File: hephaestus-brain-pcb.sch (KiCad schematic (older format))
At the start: 10 parts, among them J1 Barrel_Jack, J2 ItsyBitsy, J3 ItsyBitsy, J4 Conn_01x03_Male, J5 Conn_01x03_Male, J6 Conn_01x03_Male, J7 Conn_01x03_Male, U1 74126

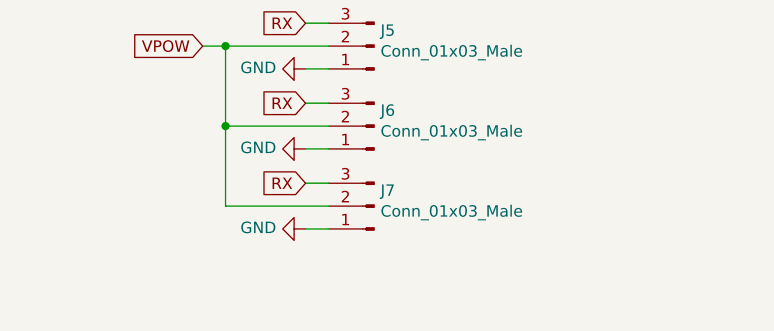
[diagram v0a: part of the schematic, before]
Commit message: Added homing switch connector
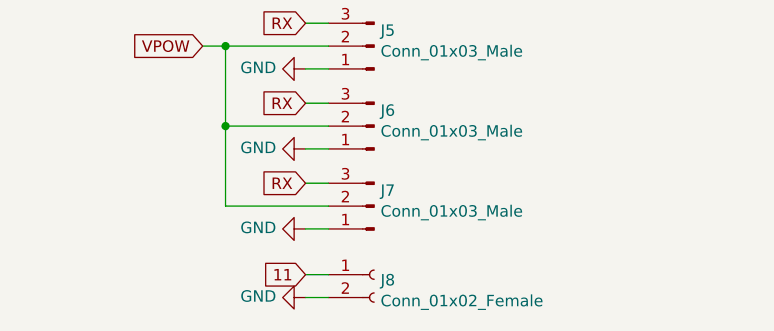
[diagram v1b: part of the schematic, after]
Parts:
- added J8: Conn_01x02_Female, Connector_PinSocket_2.54mm:PinSocket_1x02_P2.54mm_Vertical, symbol Connector:Conn_01x02_Female
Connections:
- net 11: now also J8.1 (Pin_1)
- net GND: now also J8.2 (Pin_2)
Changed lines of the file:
@@
 	4300 4850 4750 4850
 Connection ~ 4300 4500
+$Comp
+L Connector:Conn_01x02_Female J8
+U 1 1 5F188735
+P 4950 5150
+F 0 "J8" H 4978 5126 50  0000 L CNN
+F 1 "Conn_01x02_Female" H 4978 5035 50  0000 L CNN
+F 2 "Connector_PinSocket_2.54mm:PinSocket_1x02_P2.54mm_Vertical" H 4950 5150 50  0001 C CNN
+F 3 "~" H 4950 5150 50  0001 C CNN
+	1    4950 5150
+	1    0    0    -1
+$EndComp
+$Comp
+L power:GND #PWR0104
+U 1 1 5F18915B
+P 4650 5250
+F 0 "#PWR0104" H 4650 5000 50  0001 C CNN
+F 1 "GND" V 4655 5122 50  0000 R CNN
+F 2 "" H 4650 5250 50  0001 C CNN
+F 3 "" H 4650 5250 50  0001 C CNN
+	1    4650 5250
+	0    1    -1   0
+$EndComp
+Text GLabel 4650 5150 0    50   Input ~ 0
+11
+Wire Wire Line
+	4750 5150 4650 5150
+Wire Wire Line
+	4650 5250 4750 5250
 $EndSCHEMATC

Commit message: Added switch, button.
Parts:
- removed J8: Conn_01x02_Female, Connector_PinSocket_2.54mm:PinSocket_1x02_P2.54mm_Vertical, symbol Connector:Conn_01x02_Female
- added J8: Conn_01x03_Male, Connector_PinSocket_2.54mm:PinSocket_1x03_P2.54mm_Vertical, symbol Connector:Conn_01x03_Male
- added SW1: SW_SPDT, Button_Switch_THT:SW_Slide_1P2T_CK_OS102011MS2Q, symbol Switch:SW_SPDT
- added SW2, SW3: SW_SPST, Button_Switch_THT:SW_PUSH_6mm, symbol Switch:SW_SPST
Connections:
- wire segments 54 -> 63
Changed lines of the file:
@@
 Connection ~ 4300 4500
-$Comp
-L Connector:Conn_01x02_Female J8
-U 1 1 5F188735
-P 4950 5150
-F 0 "J8" H 4978 5126 50  0000 L CNN
-F 1 "Conn_01x02_Female" H 4978 5035 50  0000 L CNN
-F 2 "Connector_PinSocket_2.54mm:PinSocket_1x02_P2.54mm_Vertical" H 4950 5150 50  0001 C CNN
-F 3 "~" H 4950 5150 50  0001 C CNN
-	1    4950 5150
-	1    0    0    -1
-$EndComp
 $Comp
 L power:GND #PWR0104
@@
 	0    1    -1   0
 $EndComp
-Text GLabel 4650 5150 0    50   Input ~ 0
+Text GLabel 3050 4000 2    50   Input ~ 0
 11
 Wire Wire Line
@@
 Wire Wire Line
 	4650 5250 4750 5250
+$Comp
+L Switch:SW_SPST SW2
+U 1 1 5F19DD94
+P 2700 4000
+F 0 "SW2" H 2700 4235 50  0000 C CNN
+F 1 "SW_SPST" H 2700 4144 50  0000 C CNN
+F 2 "Button_Switch_THT:SW_PUSH_6mm" H 2700 4000 50  0001 C CNN
+F 3 "~" H 2700 4000 50  0001 C CNN
+	1    2700 4000
+	1    0    0    -1
+$EndComp
+$Comp
+L power:GND #PWR0106
+U 1 1 5F19E164
+P 2400 4000
+F 0 "#PWR0106" H 2400 3750 50  0001 C CNN
+F 1 "GND" V 2405 3872 50  0000 R CNN
+F 2 "" H 2400 4000 50  0001 C CNN
+F 3 "" H 2400 4000 50  0001 C CNN
+	1    2400 4000
+	0    1    -1   0
+$EndComp
+$Comp
+L power:GND #PWR0108
+U 1 1 5F19E536
+P 2400 3150
+F 0 "#PWR0108" H 2400 2900 50  0001 C CNN
+F 1 "GND" V 2405 3022 50  0000 R CNN
+F 2 "" H 2400 3150 50  0001 C CNN
+F 3 "" H 2400 3150 50  0001 C CNN
+	1    2400 3150
+	0    1    -1   0
+$EndComp
+Text GLabel 2950 3050 2    50   Input ~ 0
+10
+Wire Wire Line
+	3050 4000 2900 4000
+Wire Wire Line
+	2500 4000 2400 4000
+$Comp
+L Switch:SW_SPST SW3
+U 1 1 5F1ACAE6
+P 2700 4350
+F 0 "SW3" H 2700 4585 50  0000 C CNN
+F 1 "SW_SPST" H 2700 4494 50  0000 C CNN
+F 2 "Button_Switch_THT:SW_PUSH_6mm" H 2700 4350 50  0001 C CNN
+F 3 "~" H 2700 4350 50  0001 C CNN
+	1    2700 4350
+	1    0    0    -1
+$EndComp
+$Comp
+L power:GND #PWR0110
+U 1 1 5F1ACAF8
+P 2400 4350
+F 0 "#PWR0110" H 2400 4100 50  0001 C CNN
+F 1 "GND" V 2405 4222 50  0000 R CNN
+F 2 "" H 2400 4350 50  0001 C CNN
+F 3 "" H 2400 4350 50  0001 C CNN
+	1    2400 4350
+	0    1    -1   0
+$EndComp
+Wire Wire Line
+	3050 4350 2900 4350
+Wire Wire Line
+	2500 4350 2400 4350
+Text GLabel 3050 4350 2    50   Input ~ 0
+9
+$Comp
+L Connector:Conn_01x03_Male J8
+U 1 1 5F1B3FC7
+P 6600 3700
+F 0 "J8" H 6572 3632 50  0000 R CNN
+F 1 "Conn_01x03_Male" H 6572 3723 50  0000 R CNN
+F 2 "Connector_PinSocket_2.54mm:PinSocket_1x03_P2.54mm_Vertical" H 6600 3700 50  0001 C CNN
+F 3 "~" H 6600 3700 50  0001 C CNN
+	1    6600 3700
+	-1   0    0    1
+$EndComp
+Text GLabel 6300 3700 0    50   Input ~ 0
+USB
+$Comp
+L power:GND #PWR0112
+U 1 1 5F1B3FCE
+P 6300 3800
+F 0 "#PWR0112" H 6300 3550 50  0001 C CNN
+F 1 "GND" V 6305 3672 50  0000 R CNN
+F 2 "" H 6300 3800 50  0001 C CNN
+F 3 "" H 6300 3800 50  0001 C CNN
+	1    6300 3800
+	0    1    -1   0
+$EndComp
+Wire Wire Line
+	6400 3600 6300 3600
+Wire Wire Line
+	6400 3700 6300 3700
+Wire Wire Line
+	6400 3800 6300 3800
+Text GLabel 6300 3600 0    50   Input ~ 0
+13
+$Comp
+L Switch:SW_SPDT SW1
+U 1 1 5F1BB884
+P 2700 3150
+F 0 "SW1" H 2700 3435 50  0000 C CNN
+F 1 "SW_SPDT" H 2700 3344 50  0000 C CNN
+F 2 "Button_Switch_THT:SW_Slide_1P2T_CK_OS102011MS2Q" H 2700 3150 50  0001 C CNN
+F 3 "~" H 2700 3150 50  0001 C CNN
+	1    2700 3150
+	1    0    0    -1
+$EndComp
+Wire Wire Line
+	2500 3150 2400 3150
+Wire Wire Line
+	2950 3050 2900 3050
 $EndSCHEMATC
